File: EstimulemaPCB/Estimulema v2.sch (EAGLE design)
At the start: 158 parts, among them IC3 74AC14N, IC4 ISO7240S, J1 JUMPERS12MM, J2 J15MM, J3 J_7MM, J4 JUMPERS5MM, J5 JUMPERS7MM, J6 J7MM, K2 HC-06, Q17 TIP48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

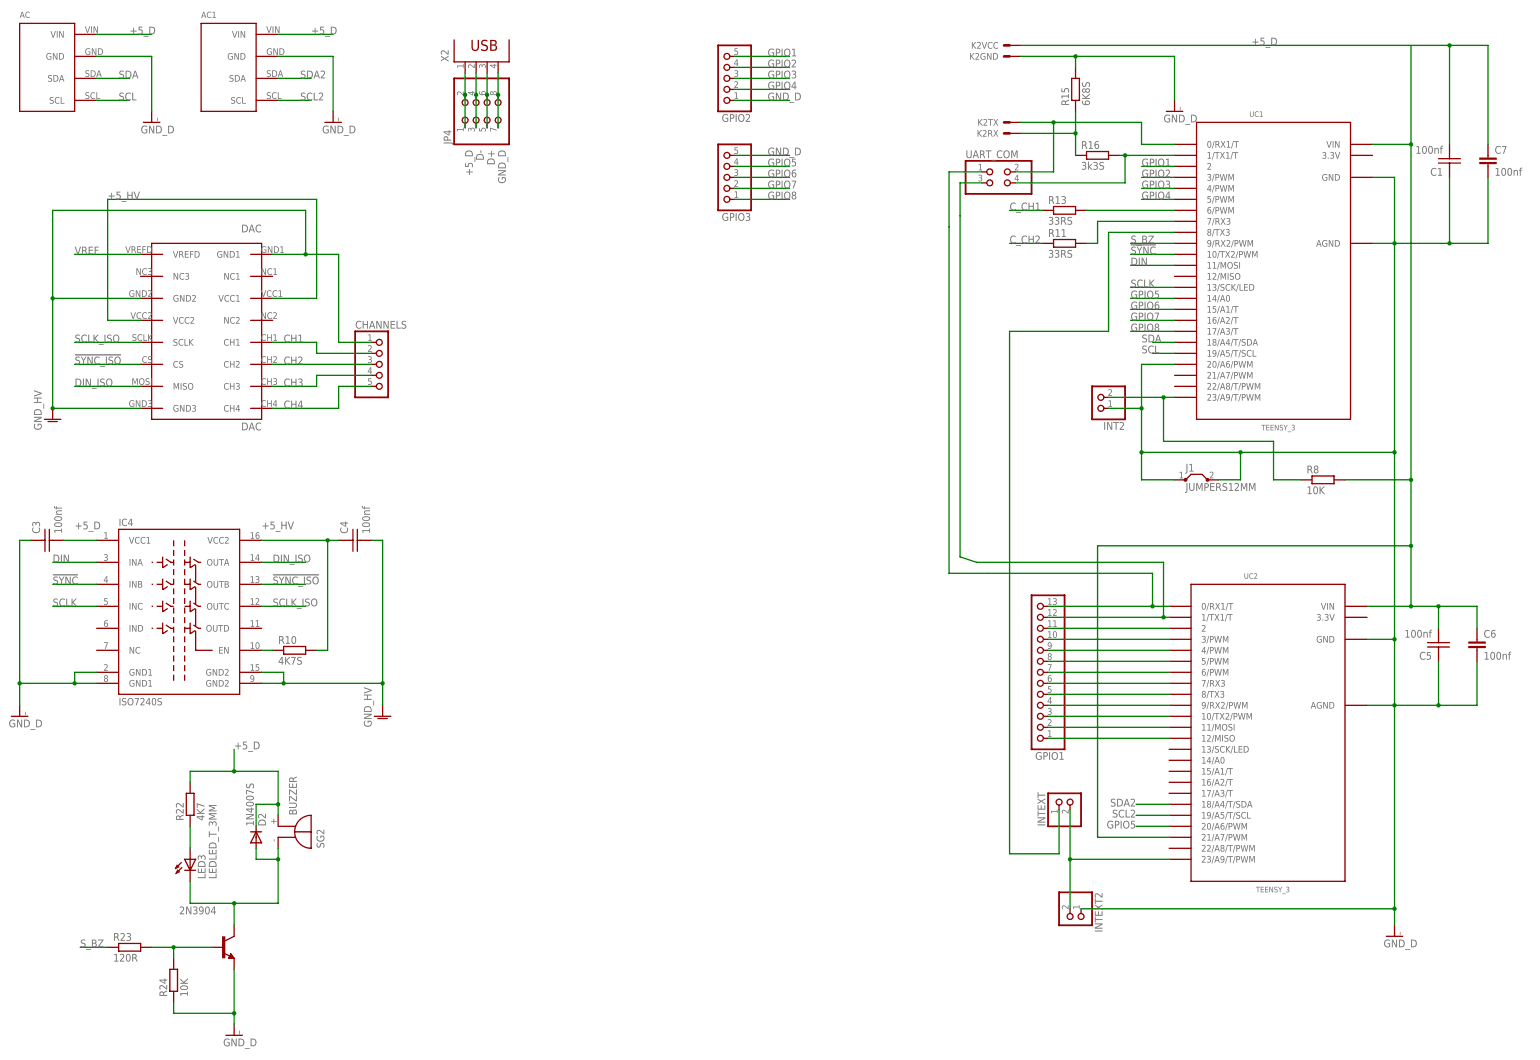
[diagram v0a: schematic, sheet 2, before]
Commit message: final version working, teste OK!!
Updates:
1. Estimulema firmware: 
beep feature was remove of stim function
Cronaxie: this function was remove of firmware and instead it was placed the calibration function for activate the accelerate acquisition.

Other small fixes.

2. Accel firmware: updates in serial communications and add functions for data flow control

3. Add new version of firmware loadcell

4. add libraries used in inos firmware
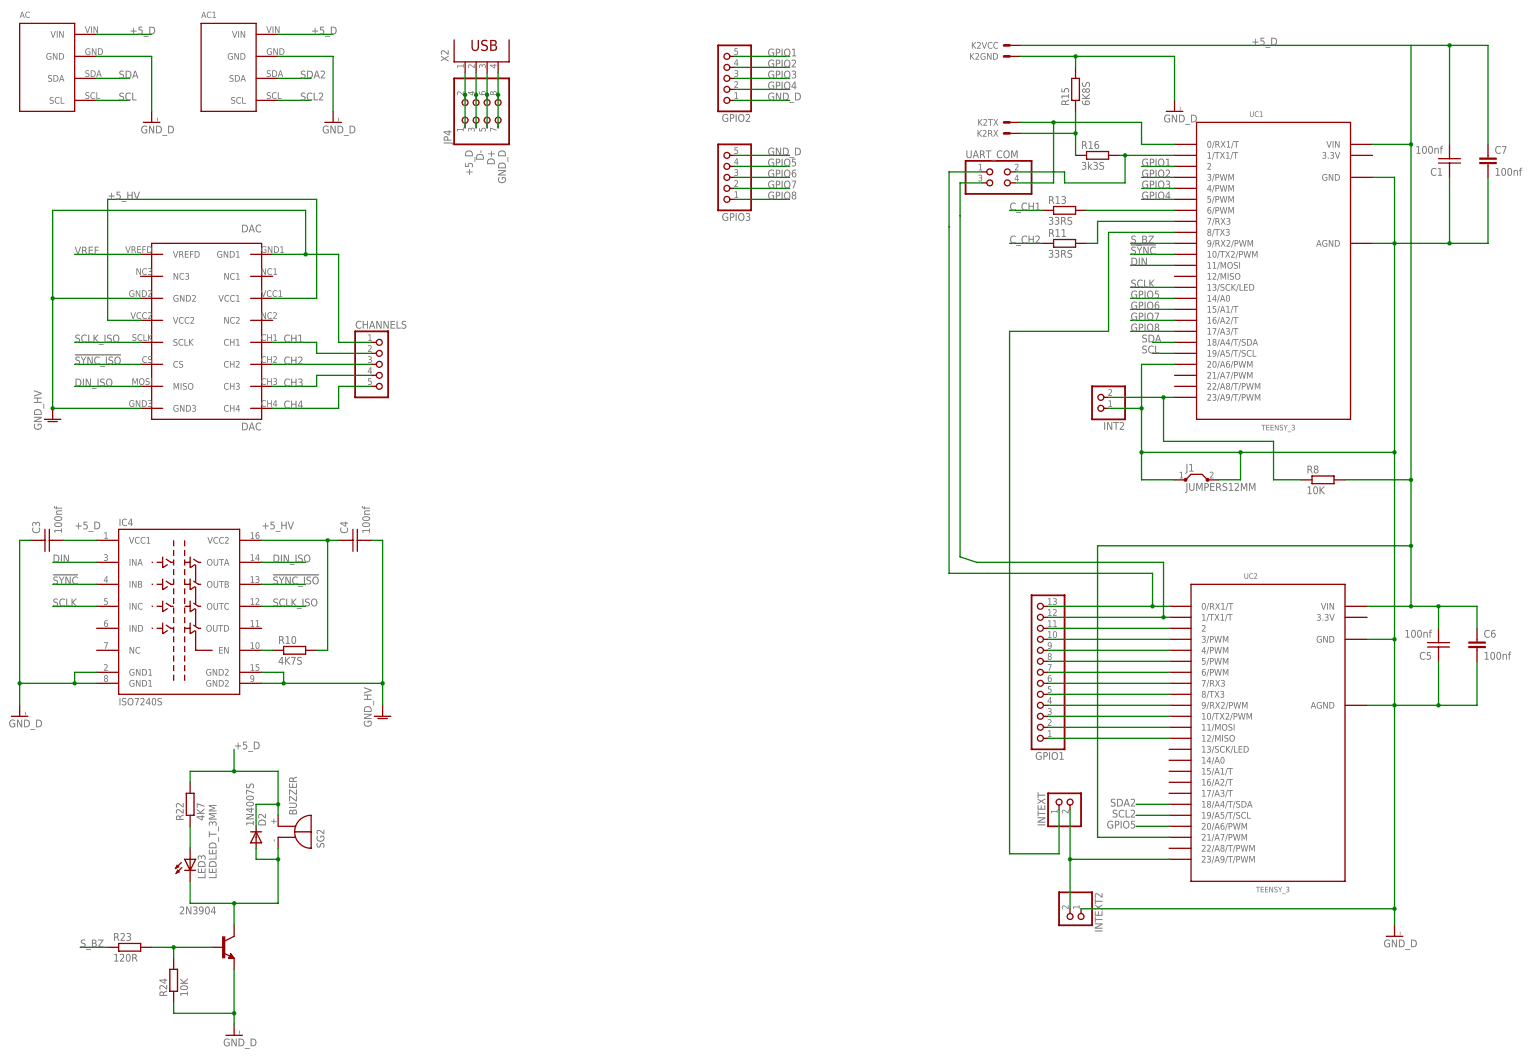
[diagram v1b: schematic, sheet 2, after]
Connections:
- net N$36: now also UART_COM.2; no longer UART_COM.4
- net N$38: now also UART_COM.4; no longer UART_COM.2
